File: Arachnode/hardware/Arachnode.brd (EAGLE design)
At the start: 71.1 x 33.7 mm, 32 parts, among them J1 PINHEAD-17-REV, J2 PINHEAD-17-REV, U1 BQ24210

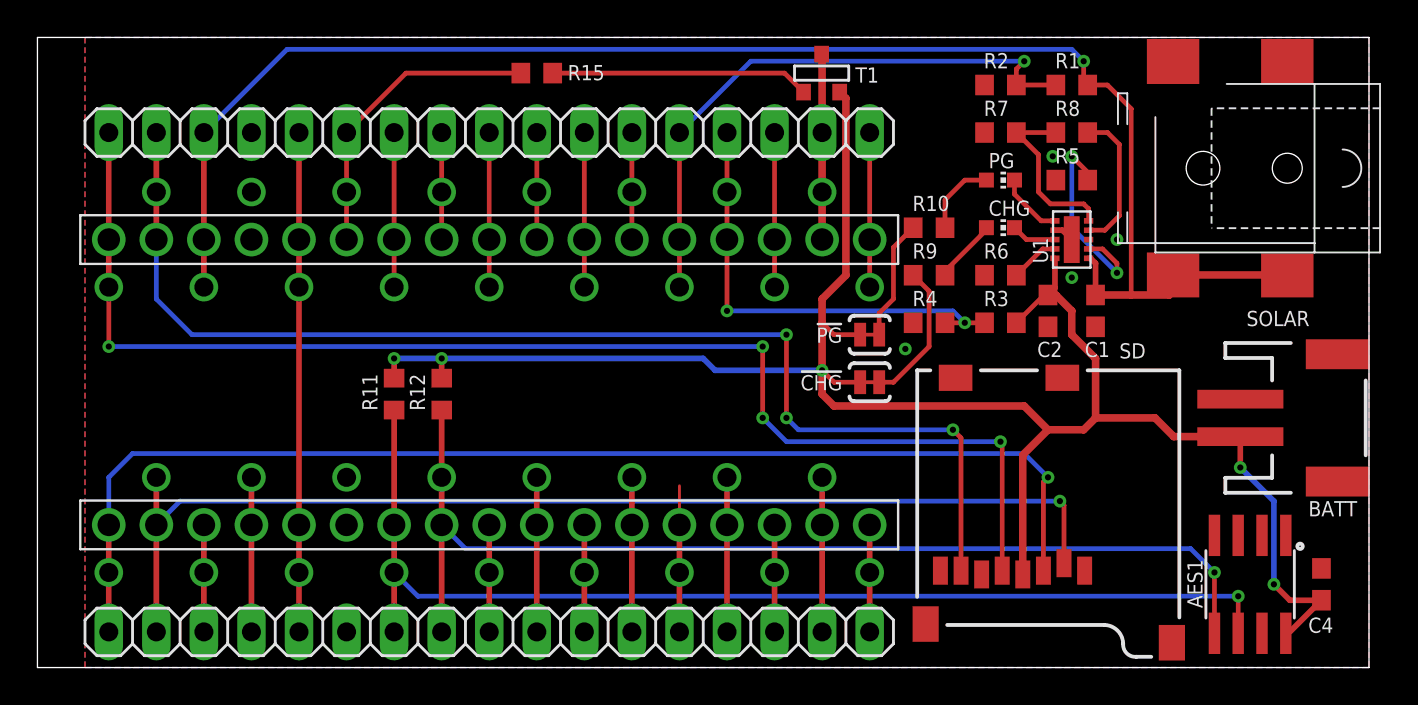
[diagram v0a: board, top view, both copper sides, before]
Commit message: Fixed the Arachnode so it's got triple row headers on the passthroughs
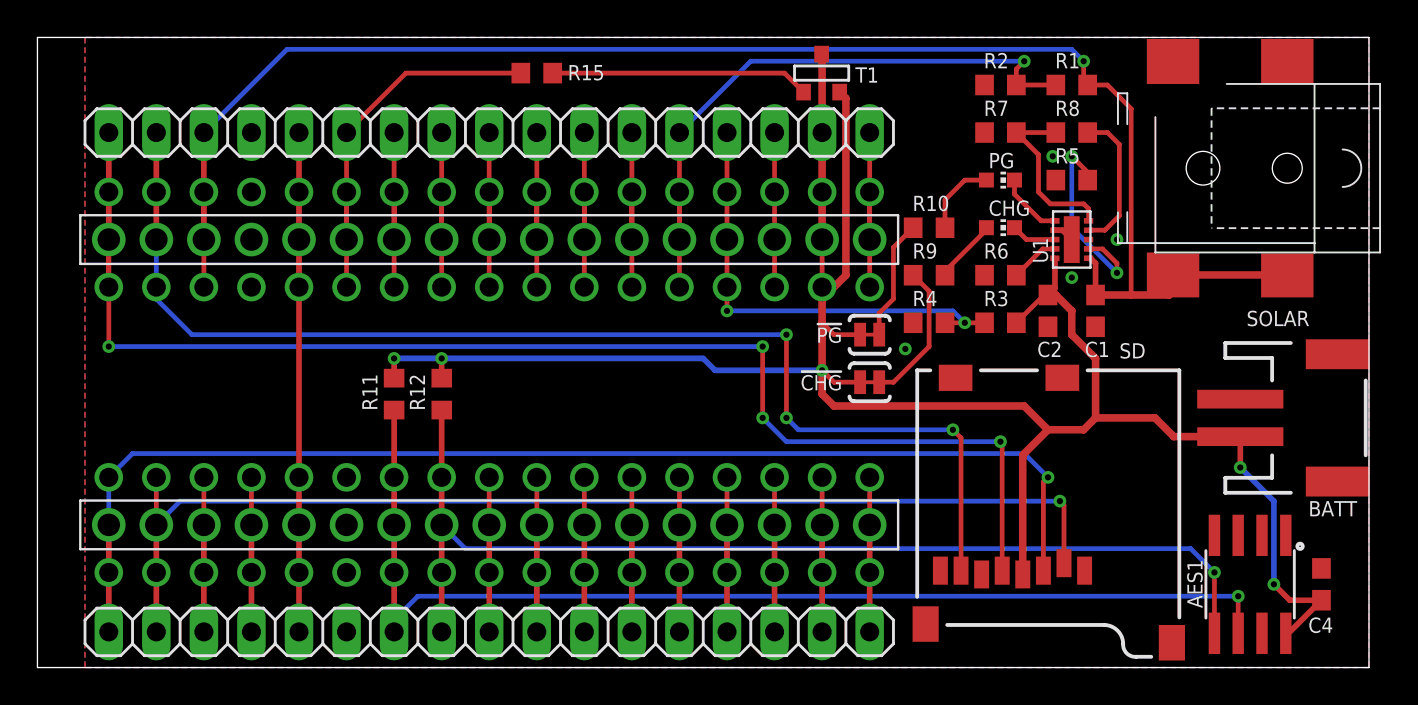
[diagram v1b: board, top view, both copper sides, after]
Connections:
- net +5V: now also J2.40
- net 3V3: now also J2.50
- net A0: now also J2.48
- net A1: now also J2.47
- net A2: now also J2.46
- net A3: now also J2.45
- net A4: now also J2.44
- net A5: now also J2.43
- net AREF: now also J2.49
- net D0: now also J1.38
- net D1: now also J1.37
- net D4: now also J1.43
- net D5: now also J1.44
- net D6: now also J1.45
- net D7: now also J1.46
- net ESP_RST: now also J2.42
- net GND: now also J1.40, J2.38
- net IO10: now also J1.49
- net IO11: now also J1.50
- net IO12: now also J1.51
- net IO13: now also J2.51
- net IO8: now also J1.47
- net IO9: now also J1.48
- net MISO: now also J2.36
- net MOSI: now also J1.35
- net RESET: now also J1.39, J2.39
- net SCK: now also J2.35
- net SCL: now also J1.42
- net SDA: now also J1.41
- net SS: now also J1.36
- net TOUT: now also J2.41
- net VIN: now also J2.37
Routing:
- net SCK: track 70.3 -> 75.4 mm
- net RESET: track 26.7 -> 31.8 mm
- net ESP_RST: track 5.71 -> 10.8 mm
- net A4: track 5.71 -> 10.8 mm
- net A2: track 5.71 -> 10.8 mm
- net 3V3: track 9.92 -> 15.0 mm
- net +5V: track 16.3 -> 21.4 mm
- net IO12: track 5.71 -> 10.8 mm
- net IO10: track 5.71 -> 10.8 mm
- net IO8: track 7.80 -> 10.8 mm
- net A1: track 31.8 -> 34.3 mm
- net TOUT: track 8.25 -> 10.8 mm
- net IO13: track 8.25 -> 10.8 mm
- net A5: track 8.25 -> 10.8 mm
- net A3: track 8.25 -> 10.8 mm
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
